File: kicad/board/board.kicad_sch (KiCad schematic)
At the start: 76 parts, among them J0 Netz, J1 Conn_01x02, J2 Schütz, J3 Pilot, Q1 IRLML5203, Q2 IRLML5203

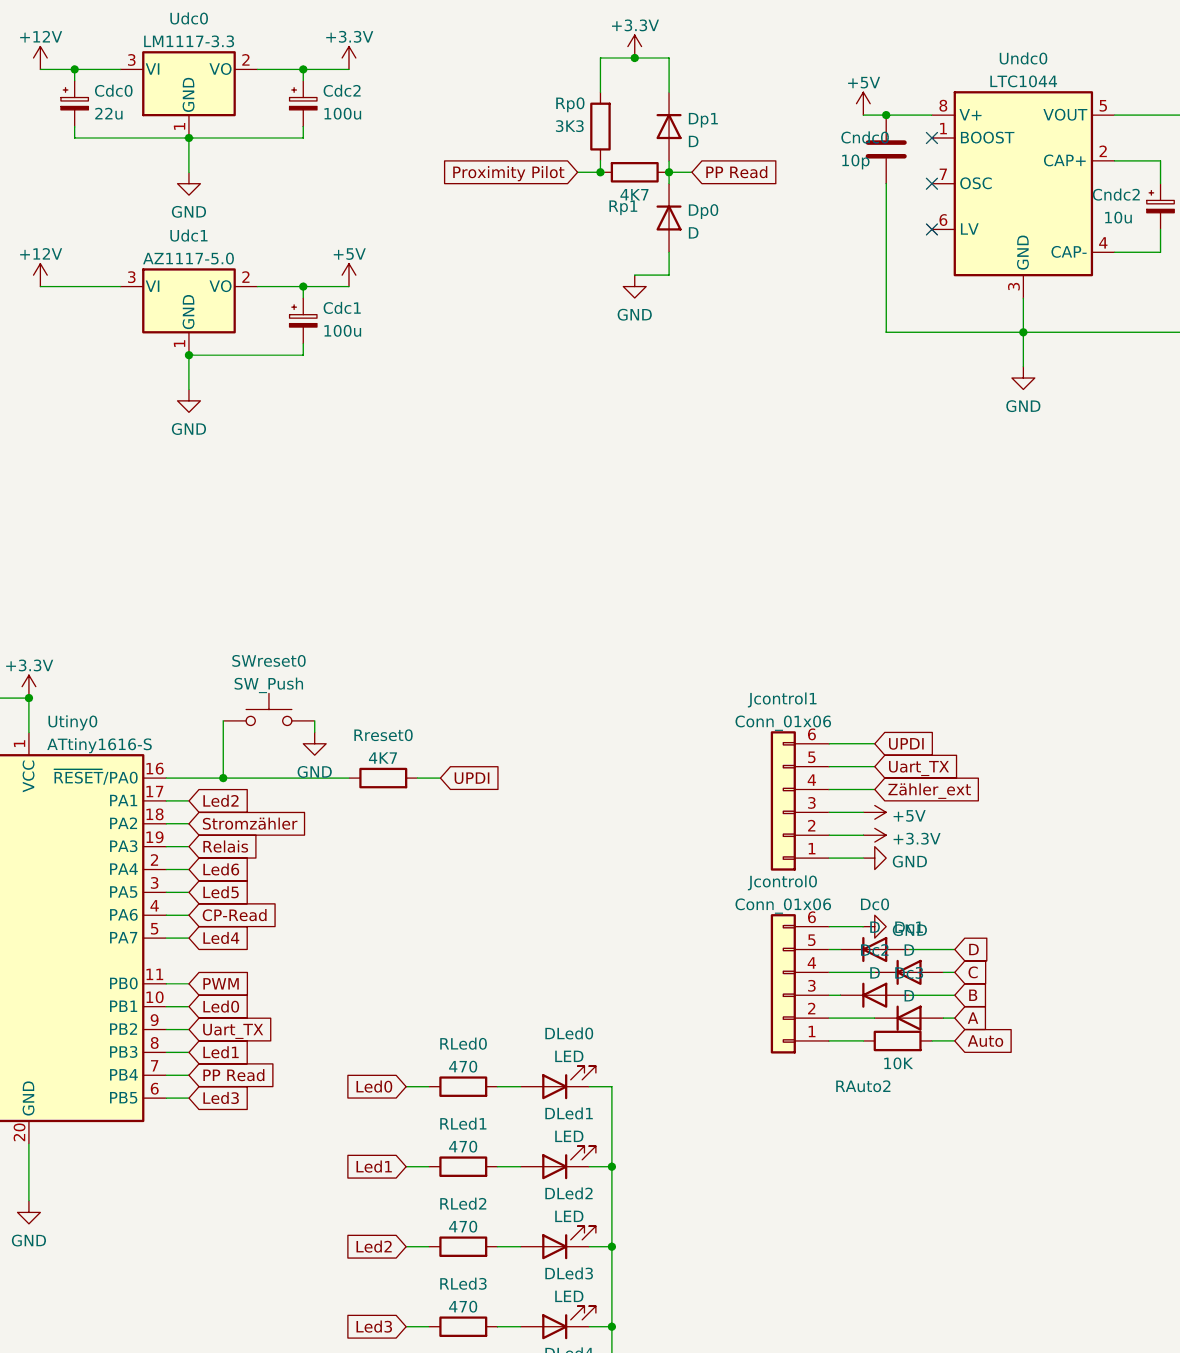
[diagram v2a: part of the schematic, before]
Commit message: hardware: korrekturen fehlerhaftes pcb
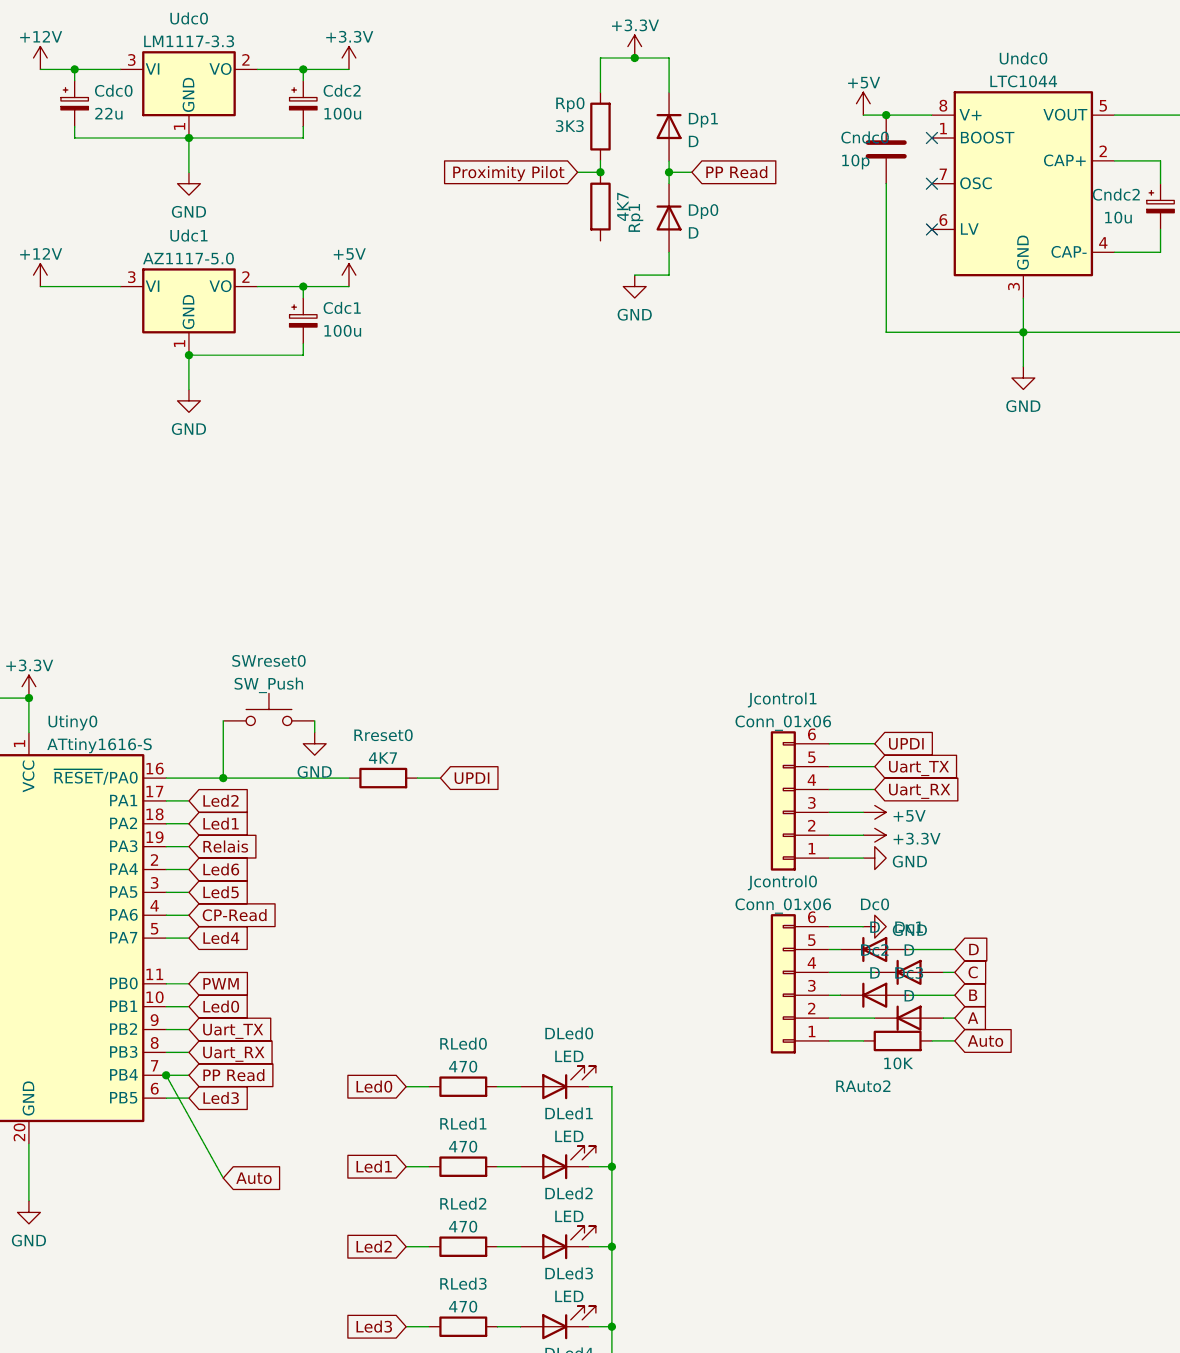
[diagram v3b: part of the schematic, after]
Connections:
- net Auto: now also Dp0.1 (K), Dp1.2 (A), Utiny0.7 (PB4)
- net Led1: now also Utiny0.18 (PA2); no longer Utiny0.8 (PB3)
- net Proximity Pilot: now also Rp1.1; no longer Rp1.2
- net Stromzähler: no longer Utiny0.18 (PA2)
- net Zähler_ext: no longer Jcontrol1.4 (Pin_4)
- removed net PP Read: Dp0.1 (K), Dp1.2 (A), Rp1.1, Utiny0.7 (PB4)
- new net Uart_RX: Jcontrol1.4 (Pin_4), Utiny0.8 (PB3)
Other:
- moved on the sheet: Rp1
